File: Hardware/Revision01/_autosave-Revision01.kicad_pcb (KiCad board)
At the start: 4 copper layers, 100 x 119.8 mm, 97 parts, among them J1 Battery connector, J21 StrainConn, J22 StrainConn, J23 StrainConn, J24 StrainConn, J25 StrainConn, J26 StrainConn, J27 StrainConn, J28 StrainConn, J4 Conn_01x03, Q3 NMOS, Q4 PMOS, Q6 PMOS, SW2 SW_SPST_LED, U1 NUCLEO-L476RG, U10 NCP1117LPST50T3G, U2 MRF89XAM9AT-I/RM, U4 ICM-45605

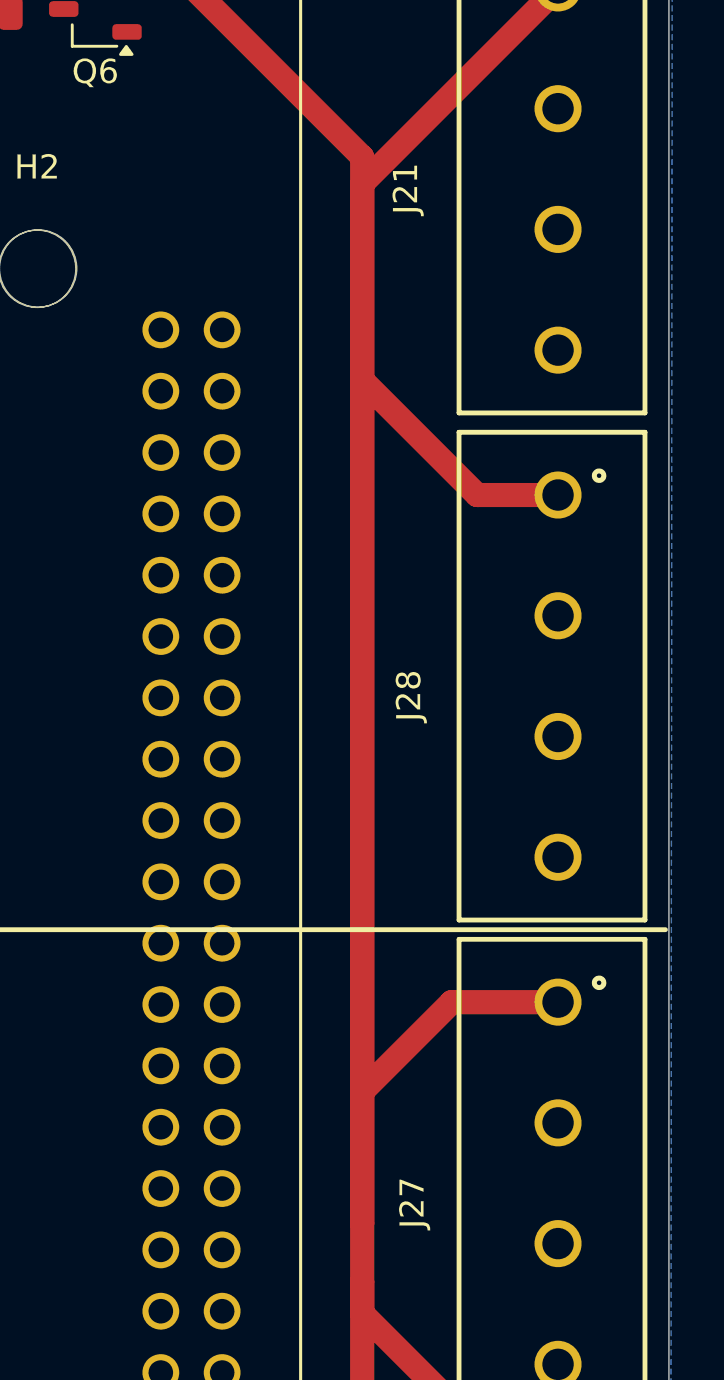
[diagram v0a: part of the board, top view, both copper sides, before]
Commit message: differential pairs setup, ready to wire on third layer.
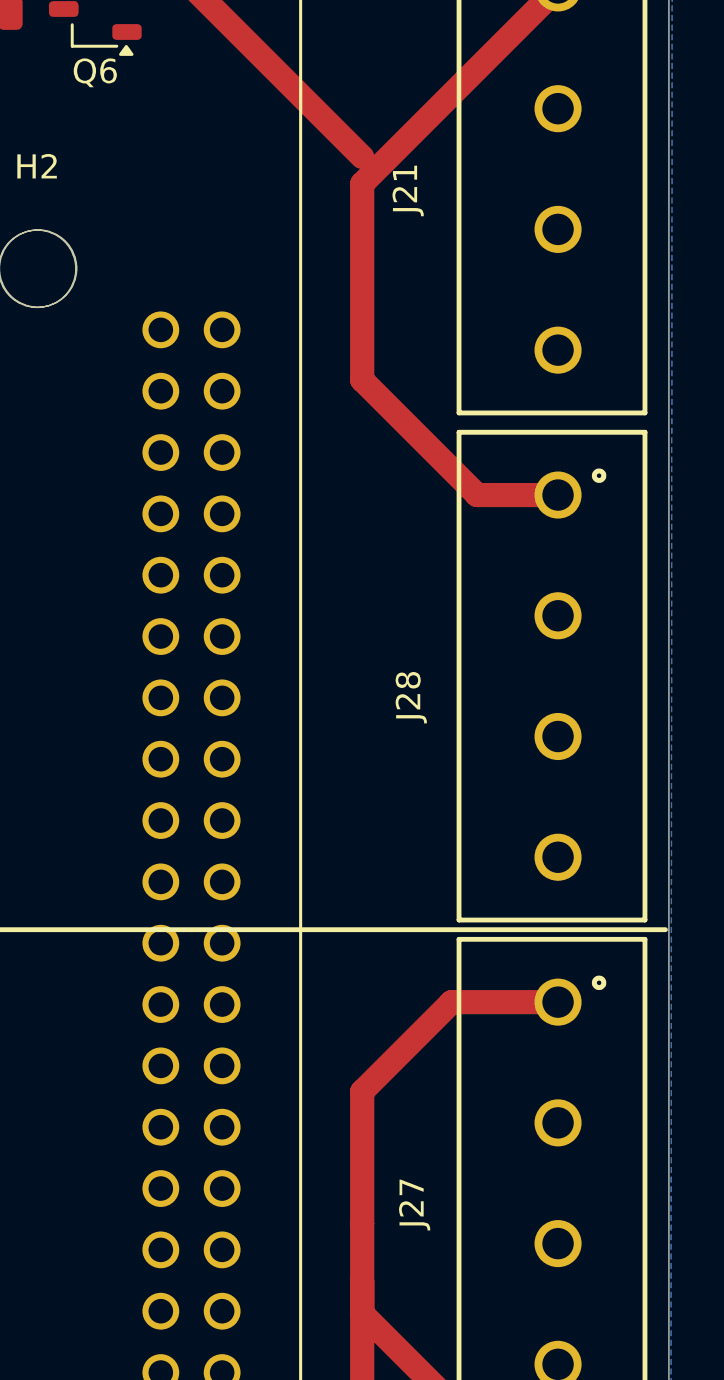
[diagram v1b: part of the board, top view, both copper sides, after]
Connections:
- R21 pad 1: /Application/AIN1_D- -> /Application/AIN1_D+
- R22 pad 1: /Application/AIN1_D+ -> /Application/AIN1_D-
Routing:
- net /Application/+StrainV: track 333.9 -> 260.3 mm
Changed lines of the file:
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@@
 			(roundrect_rratio 0.25)
 			(net 126 "unconnected-(R26-Pad1)")
-			(pintype "passive")
+			(pintype "passive+no_connect")
 		)
 		(pad "2" smd roundrect
@@
 			(roundrect_rratio 0.25)
 			(net 131 "unconnected-(R31-Pad1)")
-			(pintype "passive")
+			(pintype "passive+no_connect")
 		)
 		(pad "2" smd roundrect
@@
 			(roundrect_rratio 0.25)
 			(net 127 "unconnected-(R27-Pad1)")
-			(pintype "passive")
+			(pintype "passive+no_connect")
 		)
 		(pad "2" smd roundrect
@@
 			(roundrect_rratio 0.25)
 			(net 133 "unconnected-(R33-Pad1)")
-			(pintype "passive")
+			(pintype "passive+no_connect")
 		)
 		(pad "2" smd roundrect
@@
 			(roundrect_rratio 0.25)
 			(net 135 "unconnected-(R35-Pad1)")
-			(pintype "passive")
+			(pintype "passive+no_connect")
 		)
 		(pad "2" smd roundrect
@@
 			(layers "F.Cu" "F.Mask" "F.Paste")
 			(roundrect_rratio 0.25)
-			(net 107 "/Application/AIN1_D+")
+			(net 108 "/Application/AIN1_D-")
 			(pintype "passive")
 		)
@@
 			(roundrect_rratio 0.25)
 			(net 123 "unconnected-(R23-Pad1)")
-			(pintype "passive")
+			(pintype "passive+no_connect")
 		)
 		(pad "2" smd roundrect
@@
 			(roundrect_rratio 0.25)
 			(net 134 "unconnected-(R34-Pad1)")
-			(pintype "passive")
+			(pintype "passive+no_connect")
 		)
 		(pad "2" smd roundrect
@@
 			(roundrect_rratio 0.25)
 			(net 129 "unconnected-(R29-Pad1)")
-			(pintype "passive")
+			(pintype "passive+no_connect")
 		)
 		(pad "2" smd roundrect
@@
 			(roundrect_rratio 0.25)
 			(net 128 "unconnected-(R28-Pad1)")
-			(pintype "passive")
+			(pintype "passive+no_connect")
 		)
 		(pad "2" smd roundrect
@@
 			(roundrect_rratio 0.25)
 			(net 130 "unconnected-(R30-Pad1)")
-			(pintype "passive")
+			(pintype "passive+no_connect")
 		)
 		(pad "2" smd roundrect
@@
 			(roundrect_rratio 0.25)
 			(net 136 "unconnected-(R36-Pad1)")
-			(pintype "passive")
+			(pintype "passive+no_connect")
 		)
 		(pad "2" smd roundrect
@@
 			(layers "F.Cu" "F.Mask" "F.Paste")
 			(roundrect_rratio 0.25)
-			(net 108 "/Application/AIN1_D-")
+			(net 107 "/Application/AIN1_D+")
 			(pintype "passive")
 		)
@@
 			(roundrect_rratio 0.25)
 			(net 132 "unconnected-(R32-Pad1)")
-			(pintype "passive")
+			(pintype "passive+no_connect")
 		)
 		(pad "2" smd roundrect
@@
 			(roundrect_rratio 0.25)
 			(net 124 "unconnected-(R24-Pad1)")
-			(pintype "passive")
+			(pintype "passive+no_connect")
 		)
 		(pad "2" smd roundrect
@@
 			(roundrect_rratio 0.25)
 			(net 125 "unconnected-(R25-Pad1)")
-			(pintype "passive")
+			(pintype "passive+no_connect")
 		)
 		(pad "2" smd roundrect
@@
 	)
 	(segment
-		(start 198.32 106.584)
-		(end 198.32 77.12)
-		(width 1)
-		(layer "F.Cu")
-		(net 37)
-	)
-	(segment
 		(start 198.32 114.458)
 		(end 198.32 120.3)
@@
 		(width 1)
 		(layer "F.Cu")
-		(net 37)
-	)
-	(segment
-		(start 198.32 67.8795)
-		(end 198.32 112.045)
-		(width 1)
-		(layer "F.Cu")
